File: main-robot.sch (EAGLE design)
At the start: 12 parts

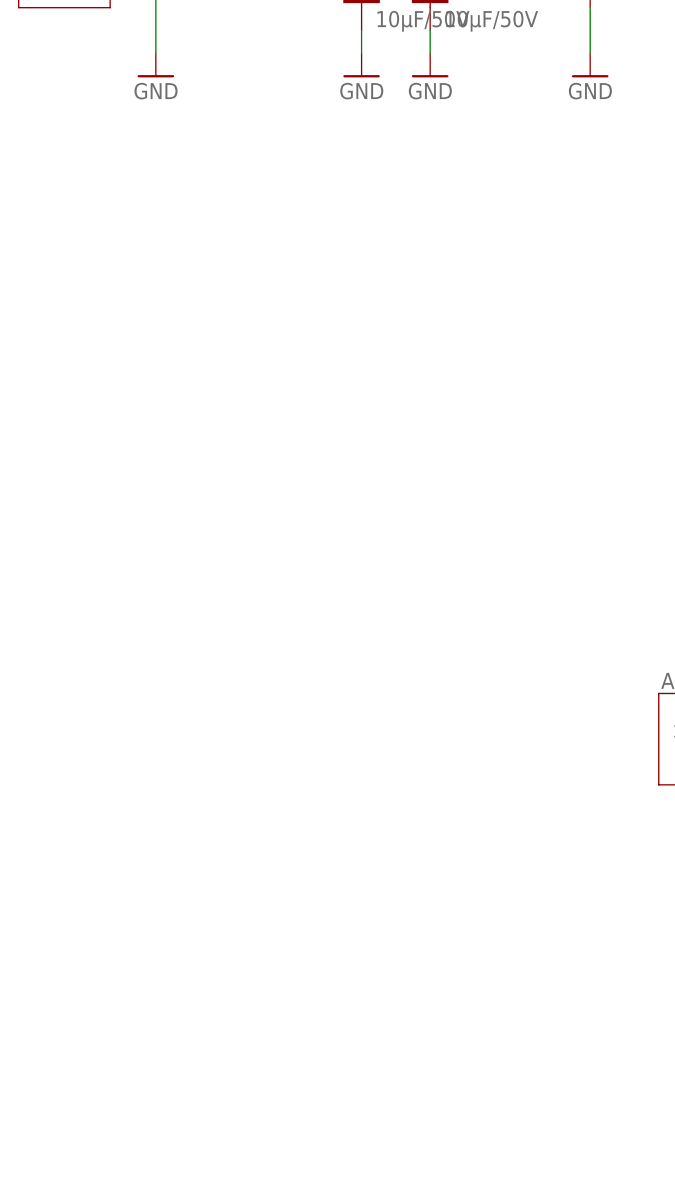
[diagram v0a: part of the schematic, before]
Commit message: Add PCB outline
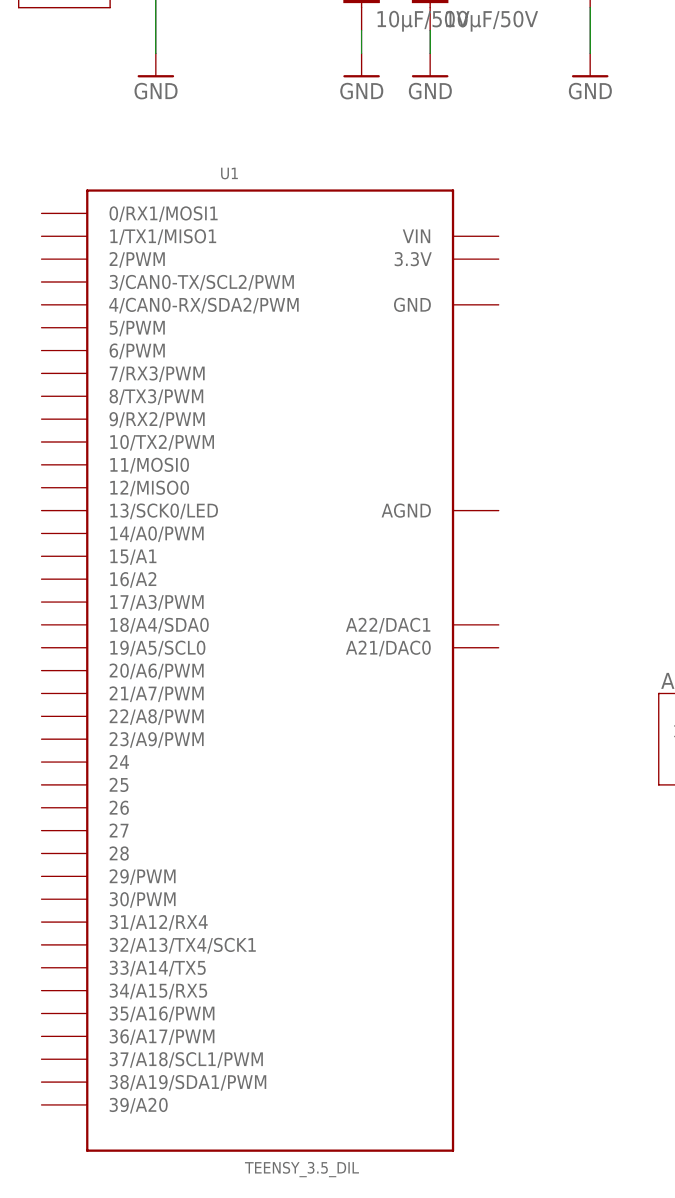
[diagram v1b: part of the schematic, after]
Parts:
- added U1: TEENSY_3.5_DIL, Teensy_libSG:TEENSY_3.5_DIL
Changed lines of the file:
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@@
 <part name="GND4" library="supply1" library_urn="urn:adsk.eagle:library:371" deviceset="GND" device=""/>
 <part name="GND5" library="supply1" library_urn="urn:adsk.eagle:library:371" deviceset="GND" device=""/>
+<part name="U1" library="Teensy_libSG" deviceset="TEENSY_3.5_DIL" device=""/>
 </parts>
 <sheets>
@@
 <attribute name="VALUE" x="96.52" y="132.08" size="1.778" layer="96" rot="MR0"/>
 </instance>
+<instance part="U1" gate="G$1" x="43.18" y="68.58" smashed="yes">
+<attribute name="NAME" x="37.592" y="123.19" size="1.27" layer="95" font="vector" ratio="15"/>
+<attribute name="VALUE" x="40.386" y="12.7" size="1.27" layer="96" font="vector" ratio="15"/>
+</instance>
 </instances>

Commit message: brd: rpi placement
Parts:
- added SV1: (no value), con-lsta:FE20-2
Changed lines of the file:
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@@
 <part name="GND5" library="supply1" library_urn="urn:adsk.eagle:library:371" deviceset="GND" device=""/>
 <part name="U1" library="Teensy_libSG" deviceset="TEENSY_3.5_DIL" device=""/>
+<part name="SV1" library="con-lsta" library_urn="urn:adsk.eagle:library:161" deviceset="FE20-2" device="" package3d_urn="urn:adsk.eagle:package:8184/1"/>
 </parts>
 <sheets>
@@
 <attribute name="VALUE" x="40.386" y="12.7" size="1.27" layer="96" font="vector" ratio="15"/>
 </instance>
+<instance part="SV1" gate="G$1" x="198.12" y="124.46" smashed="yes" rot="MR180">
+<attribute name="VALUE" x="194.31" y="154.94" size="1.778" layer="96" rot="MR180"/>
+<attribute name="NAME" x="194.31" y="98.298" size="1.778" layer="95" rot="MR180"/>
+</instance>
 </instances>

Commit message: progess in schematic
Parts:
- removed ARRET_URG, LIPO: XT-60, con-xt:XT-60
- added AR-URG-1, AR-URG-2, LIPO+, LIPO-: TPPAD1-20Y, testpad:TPPAD1-20Y
- added C10, C8: 100nF, resistor:C-EUC0805
- added C7: 10nF, resistor:C-EUC0805
- added C9: 270µF, resistor:CPOL-EUE3.5-8
- added CON1, CON2: AX12, con-molex-dynamixel:AX12
- added CON3: GENERIC-3PIN53253, con-molex-dynamixel:GENERIC-3PIN53253
- added DISPLAY, ENC_D, ENC_G: JST-04TOP, con-jst-gh:JST-04TOP
- added EXT_1: JST-06SIDE, con-jst-gh:JST-06SIDE
- added EXT_2: JST-06TOP, con-jst-gh:JST-06TOP
- added JUMPER: JST-02SIDE, con-jst-gh:JST-02SIDE
- added MOTOR: (no value), pinhead:PINHD-1X6
- added R1, R2, R3, R4, R8: 1k, resistor:R-EU_R0805
- added R5, R7: 10k, resistor:R-EU_R0805
- added R6: 820, resistor:R-EU_R0805
- added TOF_AR: JST-03SIDE, con-jst-gh:JST-03SIDE
- added TOF_ARD, TOF_ARG, TOF_AV: JST-03TOP, con-jst-gh:JST-03TOP
- added U2: VNH7100AS, h-bridge:VNH7100AS
- C1, C2, C3, C4: value 10µF/50V -> 10µF
- C5, C6: value 220µF/25V -> 220µF
- DC2: device dc-dc-converter:R-78C5.0-1.0 -> traco-power:TSR24501
- DC3: device dc-dc-converter:R-78C5.0-1.0 -> traco-power:TSR24502
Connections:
- new net +12V: AR-URG-2.TP, C3.1, C4.1, C8.1, C9.+, CON1.VCC, CON2.VCC, DC2.VIN, EXT_1.5, EXT_2.5, U2.VCC
- new net +5V/1: C6.+, DC2.VOUT, DISPLAY.4, ENC_D.4, ENC_G.4, MOTOR.4, U1.VIN
- new net +5V/2: C5.+, DC3.VOUT, SV1.2, SV1.4
- new net 3V3: EXT_1.4, EXT_2.4, R7.1, TOF_AR.2, TOF_ARD.2, TOF_ARG.2, TOF_AV.2, U1.3.3V
- new net AX12_DATA: CON1.DATA, CON2.DATA, EXT_1.2, EXT_2.2
- new net ENC_D_A: ENC_D.2
- new net ENC_D_B: ENC_D.1
- new net ENC_G_A: ENC_G.2
- new net ENC_G_B: ENC_G.1
- new net ENC_MOT_A: MOTOR.5
- new net ENC_MOT_B: MOTOR.6
- new net HV: R2.1
- new net IO_HV: R2.2
- new net IO_LV: R1.2
- new net JUMPER: R8.1
- new net LV: R1.1
- new net MOT_CS: C7.2, R5.1
- new net MOT_INA: R1.1
- new net MOT_INB: R2.1
- new net MOT_PWM: R3.1
- new net MOT_SEL: R4.1
- new net N$10: C10.2, JUMPER.1, R7.2, R8.2
- new net N$14: EXT_1.1
- new net N$15: EXT_2.1
- new net N$4: MOTOR.2, U2.OUTB
- new net N$5: R3.2, U2.PWM
- new net N$6: R2.2, U2.INB
- new net N$7: R1.2, U2.INA
- new net N$8: R4.2, U2.SEL
- new net N$9: R5.2, R6.2, U2.CS
- new net SCL: DISPLAY.1
- new net SDA: DISPLAY.2
- new net TOF_DATA: EXT_1.3, EXT_2.3, TOF_AR.3, TOF_ARD.3, TOF_ARG.3, TOF_AV.3
- net GND: now also C10.1, C3.2, C4.2, C6.-, C7.1, C8.2, C9.-, CON1.GND, CON2.GND, DC2.GND, DISPLAY.3, ENC_D.3, ENC_G.3, EXT_1.6, EXT_2.6, JUMPER.2, LIPO-.TP, MOTOR.3, R6.1, SV1.14, SV1.20, SV1.25, SV1.30, SV1.34, SV1.39, SV1.6, SV1.9, TOF_AR.1, TOF_ARD.1, TOF_ARG.1, TOF_AV.1, U1.AGND, U1.GND, U2.GNDA, U2.GNDB; no longer LIPO.(-)
- net N$1: now also AR-URG-1.TP
- net N$3: now also MOTOR.1, U2.OUTA; no longer C5.+, DC3.VOUT
- net V_LIPO: now also LIPO+.TP; no longer LIPO.(+)

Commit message: progress on schematic
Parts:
- removed C2, C3: 10µF, resistor:C-EUC1210
- removed C7: 10nF, resistor:C-EUC0805
- removed R3, R4: 1k, resistor:R-EU_R0805
- removed R5: 10k, resistor:R-EU_R0805
- removed R6: 820, resistor:R-EU_R0805
- removed U2: VNH7100AS, h-bridge:VNH7100AS
- added D2: (no value), diode:SCHOTTKY-DIODESMD
- added DC1: TSR 1-2450, traco-power:TSR24501
- added F2: MF-LSMF300, polyswitch:MF-LSMF300
- added JMP1: 0R-JUMPA, jump-0r-smd:0R-JUMPA
- added JP1: (no value), pinhead:PINHD-1X2
- added LED1, LED2, LED3, LED4, LED5, LED6, LED7, LED8: (no value), led:LEDSMT1206
- added LEDS: JST-05SIDE, con-jst-gh:JST-05SIDE
- added SW1: SWITCH-SPDT-H, switch-rs-pro:SWITCH-SPDT-H
- added SW2, SW3, SW4, SW5, SW6, SW7: PUSH-BUTTON436331045822, push-button:PUSH-BUTTON436331045822
- C1, C4: value 10µF -> 22µF; device resistor:C-EUC1210 -> resistor:C-EUC0805
- C5: device resistor:CPOL-EUE3.5-8 -> resistor:CPOL-EUD; REF_MOUSER (none) -> 667-EEE-FT1C221AP
- C6: device resistor:CPOL-EUE3.5-8 -> resistor:CPOL-EUD
- C8: value 100nF -> 22µF
- C9: value 270µF -> 220µF; device resistor:CPOL-EUE3.5-8 -> resistor:CPOL-EUD
- CON3: value GENERIC-3PIN53253 -> GENERIC-4PIN53253; device con-molex-dynamixel:GENERIC-3PIN53253 -> con-molex-dynamixel:GENERIC-4PIN53253
- R1, R2: value 1k -> 10k
- U1: value TEENSY_3.5_DIL -> TEENSY_3.5_DIL+4; device Teensy_libSG:TEENSY_3.5_DIL -> Teensy_libSG:TEENSY_3.5_DIL+4
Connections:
- net N$14 renamed EXT_DATA
- removed net MOT_CS: C7.2, R5.1
- removed net MOT_INA: R1.1
- removed net MOT_INB: R2.1
- removed net MOT_PWM: R3.1
- removed net MOT_SEL: R4.1
- removed net N$9: R5.2, R6.2, U2.CS
- new net EXT_+5V: C9.+, DC1.VOUT, JMP1-0R.1
- new net EXT_VCC: EXT_2.1, JMP1-0R.2
- new net FLAG_GPIO1: R1.1
- new net FLAG_GPIO2: R2.1
- new net INA: R1.1
- new net INB: R2.1
- new net LED_DATA: LEDS.5
- new net N$11: AR-URG-1.TP, D1.-, SW1G$1.C
- new net N$12: D2.A, JP1.2
- new net VCC: C8.1, C9.+
- new net VUSB: JP1.1, U1.VUSB
- net +12V: now also DC1.VIN, F2.1; no longer C3.1, C9.+, U2.VCC
- net +5V/1: now also D2.C, LEDS.3, LEDS.4
- net GND: now also DC1.GND, LEDS.1, LEDS.2, SW1G$2.GND; no longer C2.2, C3.2, C7.1, R6.1, U2.GNDA, U2.GNDB
- net N$1: now also SW1G$1.2; no longer AR-URG-1.TP, C2.1, D1.-
- net N$15: now also F2.2, JMP1-0R.3; no longer EXT_2.1
- net N$3: no longer U2.OUTA
- net N$4: no longer U2.OUTB
- net N$5: now also CON3.1; no longer R3.2, U2.PWM
- net N$6: now also CON3.2; no longer U2.INB
- net N$7: now also CON3.3; no longer U2.INA
- net N$8: now also CON3.4, R2.2; no longer R4.2, U2.SEL

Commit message: v1 schematics
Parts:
- added R10, R12, R14, R16, R4, R6: 10k, resistor:R-EU_R0805
- added R11, R13, R15, R17, R18, R3, R5, R9: 470, resistor:R-EU_R0805
- added RTC1: RTC, rtc-raspberry-pi:RTC
- D2: value (none) -> SS56B
- JP1: value (none) -> VUSB
- SV1: value (none) -> RPI
- SW3, SW4: value PUSH-BUTTON436331045822 -> PUSH-BUTTON; device push-button:PUSH-BUTTON436331045822 -> push-button:PUSH-BUTTON
- U1: device Teensy_libSG:TEENSY_3.5_DIL+4 -> teensy:TEENSY_3.5_DIL+4
- renumbered CON3 to FLAG
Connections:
- new net AX12_DATA_LV: U1.10/TX2/PWM, U1.9/RX2/PWM
- new net CS: R10.2, R9.1
- new net EXT_DATA_LV: U1.7/RX3/PWM, U1.8/TX3/PWM
- new net FLAG_CS: U1.16/A2
- new net FLAG_INA: U1.23/A9/PWM
- new net FLAG_INB: U1.22/A8/PWM
- new net FLAG_PWM: U1.21/A7/PWM
- new net FLAG_SEL: U1.20/A6/PWM
- new net IN_COLOR_A: R16.1, SW7.P$2, U1.25
- new net IN_COLOR_B: R14.1, SW6.P$2, U1.26
- new net IN_JUMPER: C10.2, R7.2, R8.2, U1.6/PWM
- new net LED_COLOR_A: R15.2, U1.35/A16/PWM
- new net LED_COLOR_B: R13.2, U1.36/A17/PWM
- new net LED_DATA_LV: U1.24
- new net LED_DEBUG_A: R17.2, U1.37/A18/SCL1/PWM
- new net LED_DEBUG_B: R18.2, U1.38/A19/SDA1/PWM
- new net MOT_CS: U1.17/A3/PWM
- new net MOT_INA: U1.2/PWM
- new net MOT_INB: U1.3/CAN0-TX/SCL2/PWM
- new net MOT_PWM: U1.4/CAN0-RX/SDA2/PWM
- new net MOT_SEL: U1.5/PWM
- new net N$13: R5.1, R9.2, RTC1.SDA, SV1.3
- new net N$14: RTC1.SCL, SV1.5
- new net N$16: LED2.A, R5.1
- new net N$17: LED3.A, R9.1
- new net N$18: LED4.A, R11.1
- new net N$19: LED7.A, R15.1
- new net N$20: LED5.A, R18.1
- new net N$21: LED6.A, R17.1
- new net N$9: LED1.A, R3.1, R5.2, R6.2
- new net PWM: R3.1
- new net RPI_3V3: R10.2, R12.2, R4.2, R6.2, RTC1.VIN, SV1.1
- new net RPI_IN_MATCH: R12.1, SV1.37, SW5.P$2
- new net RPI_IN_NET1: R6.1, SV1.11, SW3.P$2
- new net RPI_IN_NET2: R10.1, SV1.15, SW4.P$2
- new net RPI_IN_PWDN: R4.1, SV1.29, SW2.P$2
- new net RPI_LED_MATCH: R11.2, SV1.33
- new net RPI_LED_NET1: R5.2, SV1.13
- new net RPI_LED_NET2: R9.2, SV1.16
- new net RPI_LED_PWR: R3.2, SV1.31
- new net SCL_LV: U1.19/A5/SCL0
- new net SDA_LV: U1.18/A4/SDA0
- new net SEL: R4.1
- net 3V3: now also R14.2, R16.2
- net ENC_D_A: now also U1.11/MOSI0
- net ENC_D_B: now also U1.12/MISO0
- net ENC_G_A: now also U1.34/A15/RX5
- net ENC_G_B: now also U1.33/A14/TX5
- net ENC_MOT_A: now also U1.14/A0/PWM
- net ENC_MOT_B: now also U1.15/A1
- net FLAG_GPIO1: now also U1.31/A12/RX4
- net FLAG_GPIO2: now also U1.32/A13/TX4/SCK1
- net GND: now also LED1.C, LED2.C, LED3.C, LED4.C, LED5.C, LED6.C, LED7.C, LED8.C, R10.1, R6.1, RTC1.GND, SW2.P$1, SW3.P$1, SW4.P$1, SW5.P$1, SW6.P$1, SW7.P$1
- net JUMPER: now also JUMPER.1
- net N$10: now also LED8.A, R13.1; no longer C10.2, JUMPER.1, R7.2, R8.2
- net N$5: now also R3.2
- net N$8: now also R4.2
- net TOF_DATA: now also U1.0/RX1/MOSI1, U1.1/TX1/MISO1
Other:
- moved on the sheet: CON1, CON2, D2, DISPLAY, ENC_D, ENC_G, EXT_1, EXT_2, JP1, JUMPER, LED1, LED2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

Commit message: brd: begin routing
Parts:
- added C11, C2, C3, C7: 10µF, resistor:C-EUC0805
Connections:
- net +12V: now also C11.1, C2.1, C3.1, C7.1
- net GND: now also C11.2, C2.2, C3.2, C7.1, C7.2
- net N$13: now also C7.2
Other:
- moved on the sheet: CON1, CON2, DISPLAY, ENC_D, ENC_G, EXT_1, EXT_2, JUMPER, LEDS, TOF_AR, TOF_ARD, TOF_ARG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

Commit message: routing in progress
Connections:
- net FLAG_INA: now also U1.22/A8/PWM; no longer U1.23/A9/PWM
- net FLAG_INB: now also U1.21/A7/PWM; no longer U1.22/A8/PWM
- net FLAG_PWM: now also U1.20/A6/PWM; no longer U1.21/A7/PWM
- net FLAG_SEL: now also U1.23/A9/PWM; no longer U1.20/A6/PWM
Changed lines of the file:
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@@
 <net name="FLAG_INA" class="0">
-<segment>
-<pinref part="U1" gate="G$1" pin="23/A9/PWM"/>
-<wire x1="177.8" y1="91.44" x2="175.26" y2="91.44" width="0.1524" layer="91"/>
-<label x="175.26" y="91.44" size="1.27" layer="95" rot="R180" xref="yes"/>
-</segment>
-</net>
-<net name="FLAG_INB" class="0">
 <segment>
 <pinref part="U1" gate="G$1" pin="22/A8/PWM"/>
@@
 </segment>
 </net>
-<net name="FLAG_PWM" class="0">
+<net name="FLAG_INB" class="0">
 <segment>
 <pinref part="U1" gate="G$1" pin="21/A7/PWM"/>
@@
 </segment>
 </net>
-<net name="FLAG_SEL" class="0">
+<net name="FLAG_PWM" class="0">
 <segment>
 <pinref part="U1" gate="G$1" pin="20/A6/PWM"/>
@@
 </segment>
 </net>
+<net name="FLAG_SEL" class="0">
+<segment>
+<pinref part="U1" gate="G$1" pin="23/A9/PWM"/>
+<wire x1="177.8" y1="91.44" x2="175.26" y2="91.44" width="0.1524" layer="91"/>
+<label x="175.26" y="91.44" size="1.27" layer="95" rot="R180" xref="yes"/>
+</segment>
+</net>
